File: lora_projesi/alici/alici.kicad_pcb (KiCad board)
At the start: 4 copper layers, 88 x 102 mm, 127 parts, among them J1 USB-C, J2 SMA, J3 RJ45, J4 u.FL (ANA ANTEN), J5 12 V GIRIS, J6 LAMBA, J7 MICRO-SIM, J8 u.FL (YARDIMCI ANTEN, ISTEGE 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, K1 SRD-12VDC-SL-A, Q1 AO3401A, Q2 MMBT2222A, Q3 MMBT2222A, Q4 MMBT2222A, SW1 DUGME, U1 ESP32-S3-WROOM-1-N4, U10 SIM7600SA, U11 AP2112K-3.3, U12 ESDA6V1-5SC6, U4 RFM95W-915S2, U5 TPS62933DRLR, U6 TPS62933DRLR, U7 USBLC6-2SC6, U8 TXB0104PW, U9 W5500, Y1 25 MHz

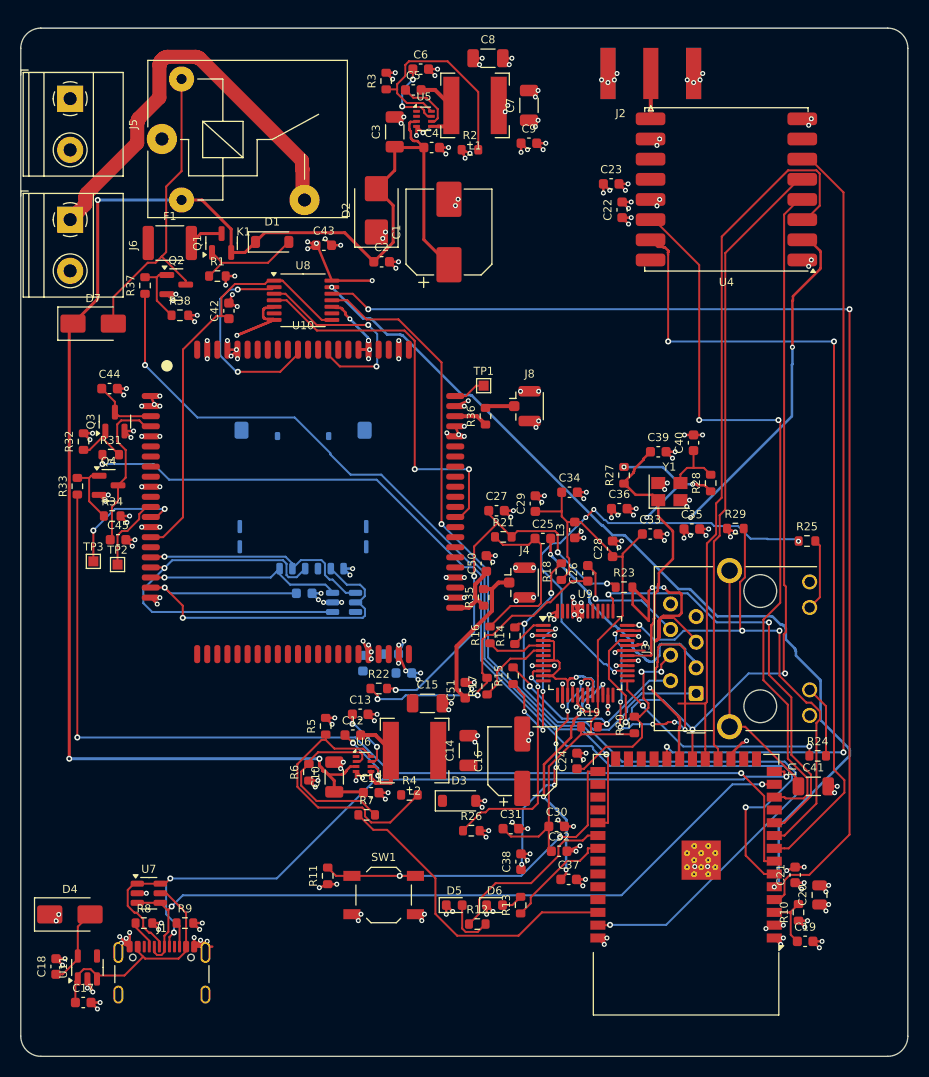
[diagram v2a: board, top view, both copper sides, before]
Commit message: Alici: lamba ve 12 V giris izleri genis, uretim dosyalari yenilendi (0 baglantisiz, 0 DRC hatasi)
Co-Authored-By: Claude Sonnet 5.5 <noreply@anthropic.com>
Claude-Session: https://claude.ai/code/session_01Q71gHQtKJ86ZE2CtYTYSwP
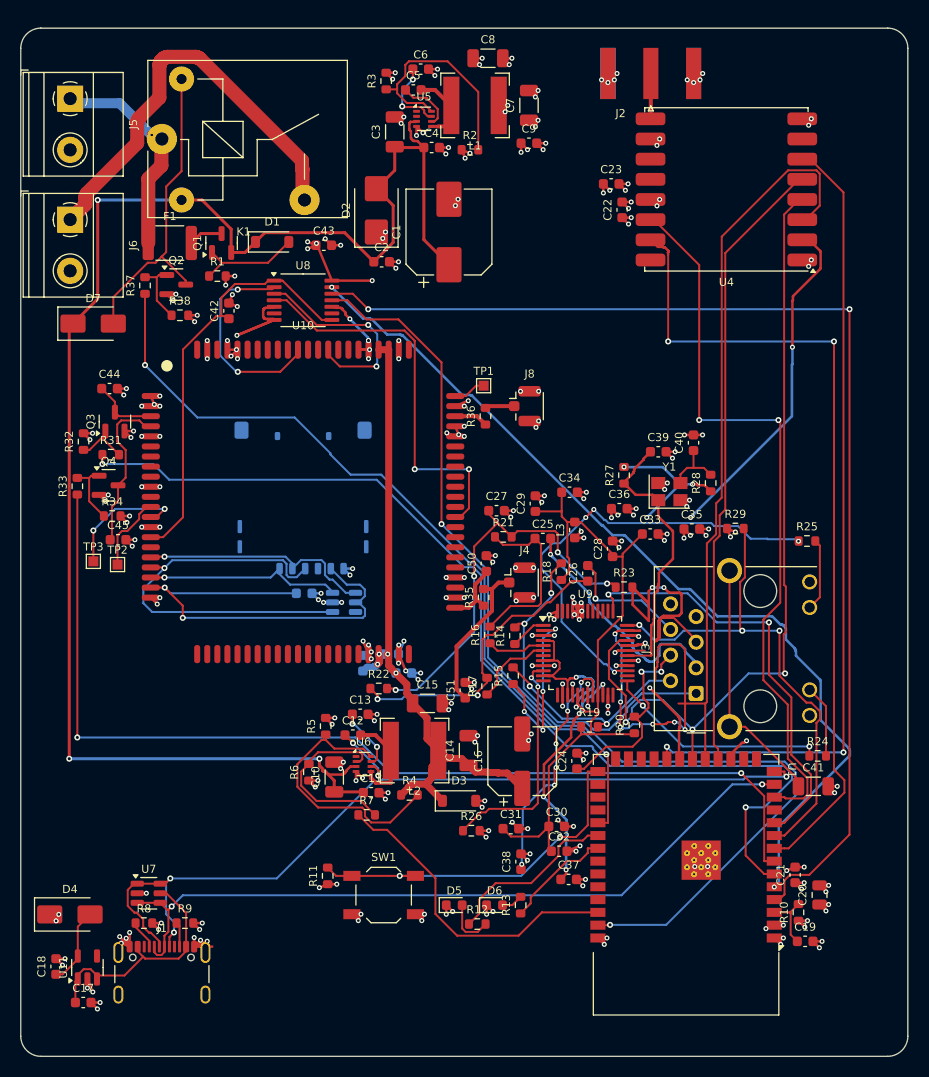
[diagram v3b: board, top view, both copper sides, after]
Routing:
- net VBAT_MOD: track 0.00 -> 67.1 mm, vias 0 -> 4
- net +12V_IN: track 0.00 -> 21.6 mm, vias 0 -> 2
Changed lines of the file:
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@@
   (segment (start 17.8593 20.3824) (end 16.9218 21.3199) (width 0.3) (layer "F.Cu") (net 6))
   (segment (start 19.9218 20.3824) (end 17.8593 20.3824) (width 0.3) (layer "F.Cu") (net 6))
+  (segment (start 14 11) (end 13.85 10.85) (width 1) (layer "F.Cu") (net 7))
+  (segment (start 13.85 10.85) (end 13.25 10.85) (width 1) (layer "F.Cu") (net 7))
+  (segment (start 12.6468 21.3199) (end 12.65 14.95) (width 1.4) (layer "F.Cu") (net 7))
+  (segment (start 12.65 14.95) (end 13.95 13.65) (width 1.4) (layer "F.Cu") (net 7))
+  (segment (start 13.95 11.05) (end 14 11) (width 1.4) (layer "F.Cu") (net 7))
+  (segment (start 13.25 10.85) (end 13 10.6) (width 1) (layer "F.Cu") (net 7))
+  (segment (start 13.95 13.65) (end 13.95 11.05) (width 1.4) (layer "F.Cu") (net 7))
+  (via (at 4.9 7) (size 0.5) (drill 0.25) (layers "F.Cu" "B.Cu") (net 7))
+  (via (at 13 10.6) (size 0.5) (drill 0.25) (layers "F.Cu" "B.Cu") (net 7))
+  (segment (start 13 10.6) (end 12.95 10.6) (width 1) (layer "B.Cu") (net 7))
+  (segment (start 5.35 7.45) (end 4.9 7) (width 1) (layer "B.Cu") (net 7))
+  (segment (start 9.8 7.45) (end 5.35 7.45) (width 1) (layer "B.Cu") (net 7))
+  (segment (start 12.95 10.6) (end 9.8 7.45) (width 1) (layer "B.Cu") (net 7))
   (segment (start 54.85 69.05) (end 54.85 68.7) (width 0.25) (layer "F.Cu") (net 8))
   (segment (start 51.9 76.2) (end 51.9 73.05) (width 0.25) (layer "F.Cu") (net 8))
@@
   (segment (start 34.1277 55.6835) (end 33.6534 55.2092) (width 0.2) (layer "B.Cu") (net 81))
   (segment (start 34.1463 57.6064) (end 34.1463 58.283) (width 0.2) (layer "B.Cu") (net 81))
+  (segment (start 38.8715 66.9877) (end 38.85 66.95) (width 0.7) (layer "F.Cu") (net 82))
+  (segment (start 36.4 62.15) (end 36.5 62.25) (width 0.7) (layer "F.Cu") (net 82))
+  (segment (start 35.55 62.3) (end 35.6 62.35) (width 0.7) (layer "F.Cu") (net 82))
+  (segment (start 40.5 74.65) (end 40.75 74.4) (width 0.7) (layer "F.Cu") (net 82))
+  (segment (start 41.1 71.3) (end 40.3 70.5) (width 0.7) (layer "F.Cu") (net 82))
+  (segment (start 38.3 65.1) (end 36.8 63.6) (width 0.7) (layer "F.Cu") (net 82))
+  (segment (start 38.3 66) (end 38.3 65.1) (width 0.7) (layer "F.Cu") (net 82))
+  (segment (start 43.7 72.45) (end 44.4147 73.1424) (width 0.7) (layer "F.Cu") (net 82))
+  (segment (start 44.35 73.05) (end 45.1 73.8) (width 0.7) (layer "F.Cu") (net 82))
+  (segment (start 35.6 62.8) (end 35.55 62.85) (width 0.7) (layer "F.Cu") (net 82))
+  (segment (start 38.4 66.15) (end 38.4 66.1) (width 0.7) (layer "F.Cu") (net 82))
+  (segment (start 37.7334 76.0684) (end 38.45 75.35) (width 0.7) (layer "F.Cu") (net 82))
+  (segment (start 42.65 72.4) (end 42.7 72.45) (width 0.7) (layer "F.Cu") (net 82))
+  (segment (start 42.3 72.4) (end 42.65 72.4) (width 0.7) (layer "F.Cu") (net 82))
+  (segment (start 35.6 62.35) (end 35.6 62.8) (width 0.7) (layer "F.Cu") (net 82))
+  (segment (start 36.5 62.25) (end 36.5 63.25) (width 0.7) (layer "F.Cu") (net 82))
+  (segment (start 40.3 68.45) (end 38.8715 66.9877) (width 0.7) (layer "F.Cu") (net 82))
+  (segment (start 41.95 72.05) (end 42.3 72.4) (width 0.7) (layer "F.Cu") (net 82))
+  (segment (start 38.85 75) (end 40.2 75) (width 0.7) (layer "F.Cu") (net 82))
+  (segment (start 36.4 62.1) (end 36.4 62.15) (width 0.7) (layer "F.Cu") (net 82))
+  (segment (start 45.1 73.8) (end 46.3 73.8) (width 0.7) (layer "F.Cu") (net 82))
+  (segment (start 40.75 74.4) (end 40.75 73.65) (width 0.7) (layer "F.Cu") (net 82))
+  (segment (start 36.5 62.1) (end 36.5 31.9) (width 0.7) (layer "F.Cu") (net 82))
+  (segment (start 40.3 70.5) (end 40.3 68.45) (width 0.7) (layer "F.Cu") (net 82))
+  (segment (start 36.5 31.9) (end 35.5 31.9) (width 0.7) (layer "F.Cu") (net 82))
+  (segment (start 36.8 63.6) (end 37.2 64) (width 0.7) (layer "F.Cu") (net 82))
+  (segment (start 38.45 75.3) (end 38.7 75.05) (width 0.7) (layer "F.Cu") (net 82))
+  (segment (start 40.2 75) (end 41.8311 76.6563) (width 0.7) (layer "F.Cu") (net 82))
+  (segment (start 36.4 62.1) (end 36.5 62.1) (width 0.7) (layer "F.Cu") (net 82))
+  (segment (start 35.55 62.95) (end 35.4 63.1) (width 0.7) (layer "F.Cu") (net 82))
+  (segment (start 41.65 72.4) (end 41.65 72.35) (width 0.7) (layer "F.Cu") (net 82))
+  (segment (start 35.55 62.1) (end 35.55 62.3) (width 0.7) (layer "F.Cu") (net 82))
+  (segment (start 47.3 73.85) (end 47.35 73.9) (width 0.7) (layer "F.Cu") (net 82))
+  (segment (start 48.25 73.9) (end 49.7484 75.4202) (width 0.7) (layer "F.Cu") (net 82))
+  (segment (start 47.35 73.9) (end 48.25 73.9) (width 0.7) (layer "F.Cu") (net 82))
+  (segment (start 36.8 63.55) (end 36.8 63.6) (width 0.7) (layer "F.Cu") (net 82))
+  (segment (start 40.8 73.6) (end 40.8 73.25) (width 0.7) (layer "F.Cu") (net 82))
+  (segment (start 46.35 73.85) (end 47.3 73.85) (width 0.7) (layer "F.Cu") (net 82))
+  (segment (start 46.3 73.8) (end 46.35 73.85) (width 0.7) (layer "F.Cu") (net 82))
+  (segment (start 41.65 72.35) (end 41.95 72.05) (width 0.7) (layer "F.Cu") (net 82))
+  (segment (start 40.5 74.7) (end 40.5 74.65) (width 0.7) (layer "F.Cu") (net 82))
+  (segment (start 41.4147 71.6674) (end 41.45 71.65) (width 0.7) (layer "F.Cu") (net 82))
+  (segment (start 41.4147 71.6674) (end 41.1 71.35) (width 0.7) (layer "F.Cu") (net 82))
+  (segment (start 40.2 75) (end 40.5 74.7) (width 0.7) (layer "F.Cu") (net 82))
+  (segment (start 44.3 73.05) (end 44.35 73.05) (width 0.7) (layer "F.Cu") (net 82))
+  (segment (start 38.4 66.1) (end 38.3 66) (width 0.7) (layer "F.Cu") (net 82))
+  (segment (start 42.7 72.45) (end 43.7 72.45) (width 0.7) (layer "F.Cu") (net 82))
+  (segment (start 38.65 66.4) (end 38.4 66.15) (width 0.7) (layer "F.Cu") (net 82))
+  (segment (start 35.55 62.85) (end 35.55 62.95) (width 0.7) (layer "F.Cu") (net 82))
+  (segment (start 40.8 73.25) (end 41.65 72.4) (width 0.7) (layer "F.Cu") (net 82))
+  (segment (start 38.7 75.05) (end 38.8 75.05) (width 0.7) (layer "F.Cu") (net 82))
+  (segment (start 35.55 62.1) (end 35.5 62.1) (width 0.7) (layer "F.Cu") (net 82))
+  (segment (start 41.85 72.05) (end 41.95 72.05) (width 0.7) (layer "F.Cu") (net 82))
+  (segment (start 38.8 75.05) (end 38.85 75) (width 0.7) (layer "F.Cu") (net 82))
+  (segment (start 41.45 71.65) (end 41.85 72.05) (width 0.7) (layer "F.Cu") (net 82))
+  (segment (start 41.1 71.35) (end 41.1 71.3) (width 0.7) (layer "F.Cu") (net 82))
+  (segment (start 40.75 73.65) (end 40.8 73.6) (width 0.7) (layer "F.Cu") (net 82))
+  (segment (start 43.7 72.45) (end 44.3 73.05) (width 0.7) (layer "F.Cu") (net 82))
+  (segment (start 38.45 75.35) (end 38.45 75.3) (width 0.7) (layer "F.Cu") (net 82))
+  (segment (start 38.65 66.75) (end 38.65 66.4) (width 0.7) (layer "F.Cu") (net 82))
+  (segment (start 38.85 66.95) (end 38.65 66.75) (width 0.7) (layer "F.Cu") (net 82))
+  (segment (start 36.5 63.25) (end 36.8 63.55) (width 0.7) (layer "F.Cu") (net 82))
+  (via (at 37.2214 63.9764) (size 0.5) (drill 0.25) (layers "F.Cu" "B.Cu") (net 82))
+  (via (at 35.55 62.1) (size 0.5) (drill 0.25) (layers "F.Cu" "B.Cu") (net 82))
+  (via (at 36.4 62.1) (size 0.5) (drill 0.25) (layers "F.Cu" "B.Cu") (net 82))
+  (via (at 35.4 63.1) (size 0.5) (drill 0.25) (layers "F.Cu" "B.Cu") (net 82))
+  (segment (start 35.925 62.1) (end 35.55 62.1) (width 0.7) (layer "B.Cu") (net 82))
+  (segment (start 34.35 63.4) (end 33.9412 63.775) (width 0.7) (layer "B.Cu") (net 82))
+  (segment (start 35 63.4) (end 34.35 63.4) (width 0.7) (layer "B.Cu") (net 82))
+  (segment (start 35.4 63.1) (end 35.15 63.35) (width 0.7) (layer "B.Cu") (net 82))
+  (segment (start 35.05 63.35) (end 35 63.4) (width 0.7) (layer "B.Cu") (net 82))
+  (segment (start 35.15 63.35) (end 35.05 63.35) (width 0.7) (layer "B.Cu") (net 82))
+  (segment (start 35.925 62.1) (end 36.4 62.1) (width 0.7) (layer "B.Cu") (net 82))
   (segment (start 14.4433 85.8238) (end 13.834 85.8238) (width 0.2) (layer "F.Cu") (net 83))
   (segment (start 6.9326 93.3547) (end 6.2395 93.3547) (width 0.2) (layer "F.Cu") (net 83))

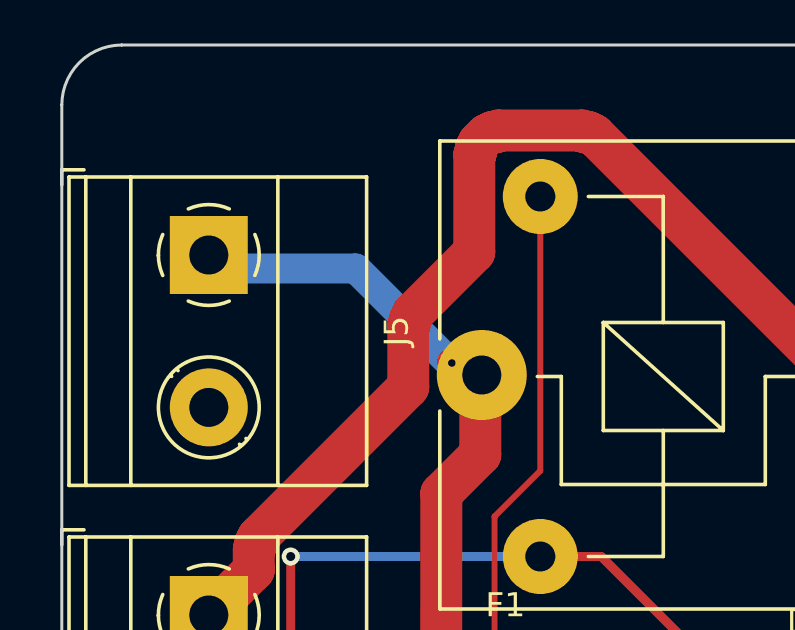
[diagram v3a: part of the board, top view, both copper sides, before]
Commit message: Alici: lamba hatti 1,4 mm viyasiz; uretim dosyalari ve site yenilendi
Co-Authored-By: Claude Sonnet 5.5 <noreply@anthropic.com>
Claude-Session: https://claude.ai/code/session_01Q71gHQtKJ86ZE2CtYTYSwP
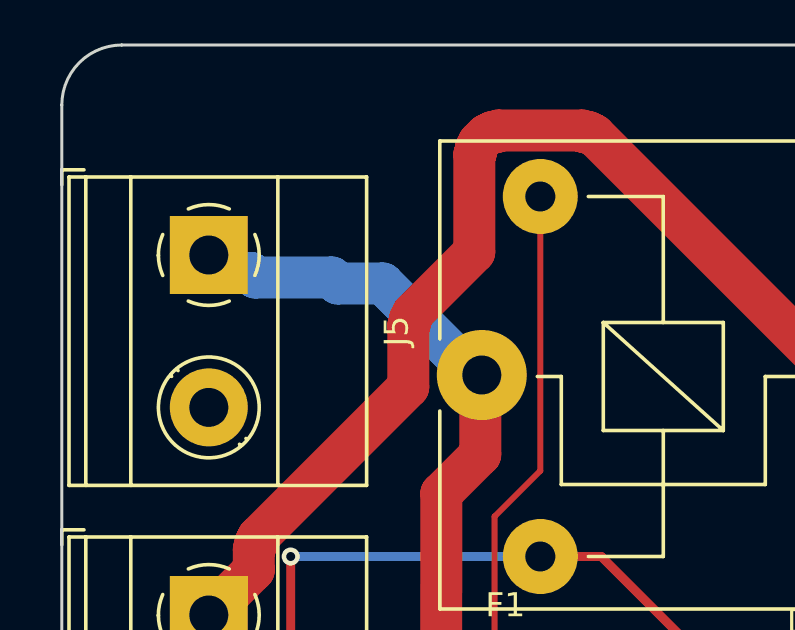
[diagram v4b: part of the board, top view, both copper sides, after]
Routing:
- net +12V_IN: vias 2 -> 0
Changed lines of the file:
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@@
   (segment (start 17.8593 20.3824) (end 16.9218 21.3199) (width 0.3) (layer "F.Cu") (net 6))
   (segment (start 19.9218 20.3824) (end 17.8593 20.3824) (width 0.3) (layer "F.Cu") (net 6))
-  (segment (start 14 11) (end 13.85 10.85) (width 1) (layer "F.Cu") (net 7))
-  (segment (start 13.85 10.85) (end 13.25 10.85) (width 1) (layer "F.Cu") (net 7))
   (segment (start 12.6468 21.3199) (end 12.65 14.95) (width 1.4) (layer "F.Cu") (net 7))
   (segment (start 12.65 14.95) (end 13.95 13.65) (width 1.4) (layer "F.Cu") (net 7))
   (segment (start 13.95 11.05) (end 14 11) (width 1.4) (layer "F.Cu") (net 7))
-  (segment (start 13.25 10.85) (end 13 10.6) (width 1) (layer "F.Cu") (net 7))
   (segment (start 13.95 13.65) (end 13.95 11.05) (width 1.4) (layer "F.Cu") (net 7))
-  (via (at 4.9 7) (size 0.5) (drill 0.25) (layers "F.Cu" "B.Cu") (net 7))
-  (via (at 13 10.6) (size 0.5) (drill 0.25) (layers "F.Cu" "B.Cu") (net 7))
-  (segment (start 13 10.6) (end 12.95 10.6) (width 1) (layer "B.Cu") (net 7))
-  (segment (start 5.35 7.45) (end 4.9 7) (width 1) (layer "B.Cu") (net 7))
-  (segment (start 9.8 7.45) (end 5.35 7.45) (width 1) (layer "B.Cu") (net 7))
-  (segment (start 12.95 10.6) (end 9.8 7.45) (width 1) (layer "B.Cu") (net 7))
+  (segment (start 9 7.75) (end 9.2 7.95) (width 1.4) (layer "B.Cu") (net 7))
+  (segment (start 13.95 10.95) (end 14 11) (width 1.4) (layer "B.Cu") (net 7))
+  (segment (start 4.9 7) (end 5.5 7.6) (width 1.4) (layer "B.Cu") (net 7))
+  (segment (start 5.5 7.6) (end 6.3 7.6) (width 1.4) (layer "B.Cu") (net 7))
+  (segment (start 10.7 7.95) (end 13.7 10.95) (width 1.4) (layer "B.Cu") (net 7))
+  (segment (start 13.7 10.95) (end 13.95 10.95) (width 1.4) (layer "B.Cu") (net 7))
+  (segment (start 9.2 7.95) (end 10.7 7.95) (width 1.4) (layer "B.Cu") (net 7))
+  (segment (start 6.3 7.6) (end 6.45 7.75) (width 1.4) (layer "B.Cu") (net 7))
+  (segment (start 6.45 7.75) (end 9 7.75) (width 1.4) (layer "B.Cu") (net 7))
   (segment (start 54.85 69.05) (end 54.85 68.7) (width 0.25) (layer "F.Cu") (net 8))
   (segment (start 51.9 76.2) (end 51.9 73.05) (width 0.25) (layer "F.Cu") (net 8))

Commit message: VBAT 4,0 V + polimer ESR sarti; gercekci simulasyonlar ve maliyet modeli
Co-Authored-By: Claude Sonnet 5.5 <noreply@anthropic.com>
Claude-Session: https://claude.ai/code/session_01Q71gHQtKJ86ZE2CtYTYSwP
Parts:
- C16: value 330uF 6,3V polimer -> 330uF 6,3V polimer ESR en fazla 40 mOhm
- R4: value 37,4k 1% -> 40,2k 1%
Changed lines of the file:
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@@
         (effects (font (size 0.8 0.8) (thickness 0.12)))
     )
-    (fp_text value "37,4k 1%" (at 0 1.43) (layer "F.Fab") hide
+    (fp_text value "40,2k 1%" (at 0 1.43) (layer "F.Fab") hide
         (effects (font (size 1 1) (thickness 0.15)))
     )
@@
         (effects (font (size 0.8 0.8) (thickness 0.12)))
     )
-    (fp_text value "330uF 6,3V polimer" (at 0 4.35 90) (layer "F.Fab") hide
-        (effects (font (size 1 1) (thickness 0.15)))
-    )
+    (fp_text value "330uF 6,3V polimer ESR en fazla 40 mOhm" (at 0 4.35 90) (layer "F.Fab") hide
+        (effects (font (size 1 1) (thickness 0.15)))
+    )

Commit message: Parca belgeleri okundu: PTC son eki, endüktör Isat, BST dielektrik, kristal sarti; BELGELER.md
Co-Authored-By: Claude Sonnet 5.5 <noreply@anthropic.com>
Claude-Session: https://claude.ai/code/session_01Q71gHQtKJ86ZE2CtYTYSwP
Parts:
- C12, C5: value 100nF 25V -> 100nF 25V X7R
- F1: value 1812L200 (2 A) -> 1812L200/16DR (2 A, 16 V)
- L1, L2: value 4,7uH 5A -> 4,7uH Isat 2,7A
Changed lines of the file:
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@@
         (effects (font (size 0.8 0.8) (thickness 0.12)))
     )
-    (fp_text value "1812L200 (2 A)" (at 0 2.65) (layer "F.Fab") hide
+    (fp_text value "1812L200/16DR (2 A, 16 V)" (at 0 2.65) (layer "F.Fab") hide
         (effects (font (size 1 1) (thickness 0.15)))
     )
@@
         (effects (font (size 0.8 0.8) (thickness 0.12)))
     )
-    (fp_text value "100nF 25V" (at 0 1.43) (layer "F.Fab") hide
+    (fp_text value "100nF 25V X7R" (at 0 1.43) (layer "F.Fab") hide
         (effects (font (size 1 1) (thickness 0.15)))
     )
@@
         (effects (font (size 0.8 0.8) (thickness 0.12)))
     )
-    (fp_text value "4,7uH 5A" (at 0 -4) (layer "F.Fab") hide
+    (fp_text value "4,7uH Isat 2,7A" (at 0 -4) (layer "F.Fab") hide
         (effects (font (size 1 1) (thickness 0.15)))
     )
@@
         (effects (font (size 0.8 0.8) (thickness 0.12)))
     )
-    (fp_text value "100nF 25V" (at 0 1.43) (layer "F.Fab") hide
+    (fp_text value "100nF 25V X7R" (at 0 1.43) (layer "F.Fab") hide
         (effects (font (size 1 1) (thickness 0.15)))
     )
@@
         (effects (font (size 0.8 0.8) (thickness 0.12)))
     )
-    (fp_text value "4,7uH 5A" (at 0 -4) (layer "F.Fab") hide
+    (fp_text value "4,7uH Isat 2,7A" (at 0 -4) (layer "F.Fab") hide
         (effects (font (size 1 1) (thickness 0.15)))
     )
